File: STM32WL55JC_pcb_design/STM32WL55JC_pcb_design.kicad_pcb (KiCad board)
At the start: 2 copper layers, 131 parts, among them IC1 STM32F051R8T6, IC2 CG2409M2, IC3 SX1276IMLTRT, IC4 CG2409M2, IC5 PCF8575TS_1,118, IC6 PCF8575TS_1,118, IC7 ATGM336H-5N31, J1 Conn_01x03, J10 Conn_01x08_Male, J11 Conn_02x02_Odd_Even, J12 Conn_01x10, J13 Conn_01x10, J14 Conn_01x10, J15 Conn_01x10, J16 Conn_Coaxial, J17 Conn_Coaxial, J18 CT3151-2, J19 CT3151-2, J2 Conn_01x03, J20 USB-A-S-F-B-TH, J21 Conn_02x02_Odd_Even, J22 Conn_01x19_Male, J23 RSP-122811-01, J3 Conn_01x03, J4 Conn_01x09, J5 Conn_01x09, J6 Conn_01x03, J7 Conn_01x09, J8 Conn_01x09, J9 Conn_02x10_Odd_Even, Q1 AO3401A, U1 PCF8574, U2 SHT30-DIS, U3 LIS3DHTR, U4 AMS1117-3.3, U5 AMS1117-5.0, Y1 32MHz, Y2 32.768kHz, Y3 32MHz

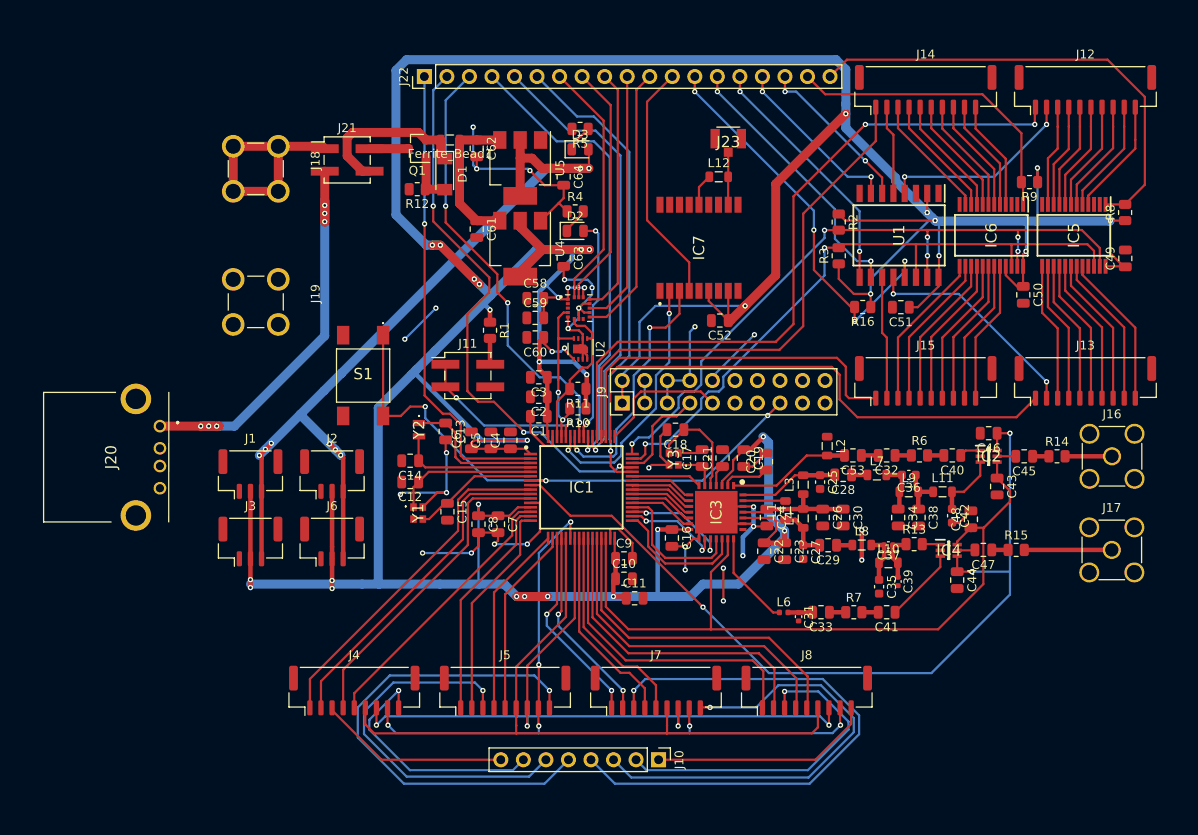
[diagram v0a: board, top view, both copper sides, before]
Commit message: Add copper fill and edge cuts
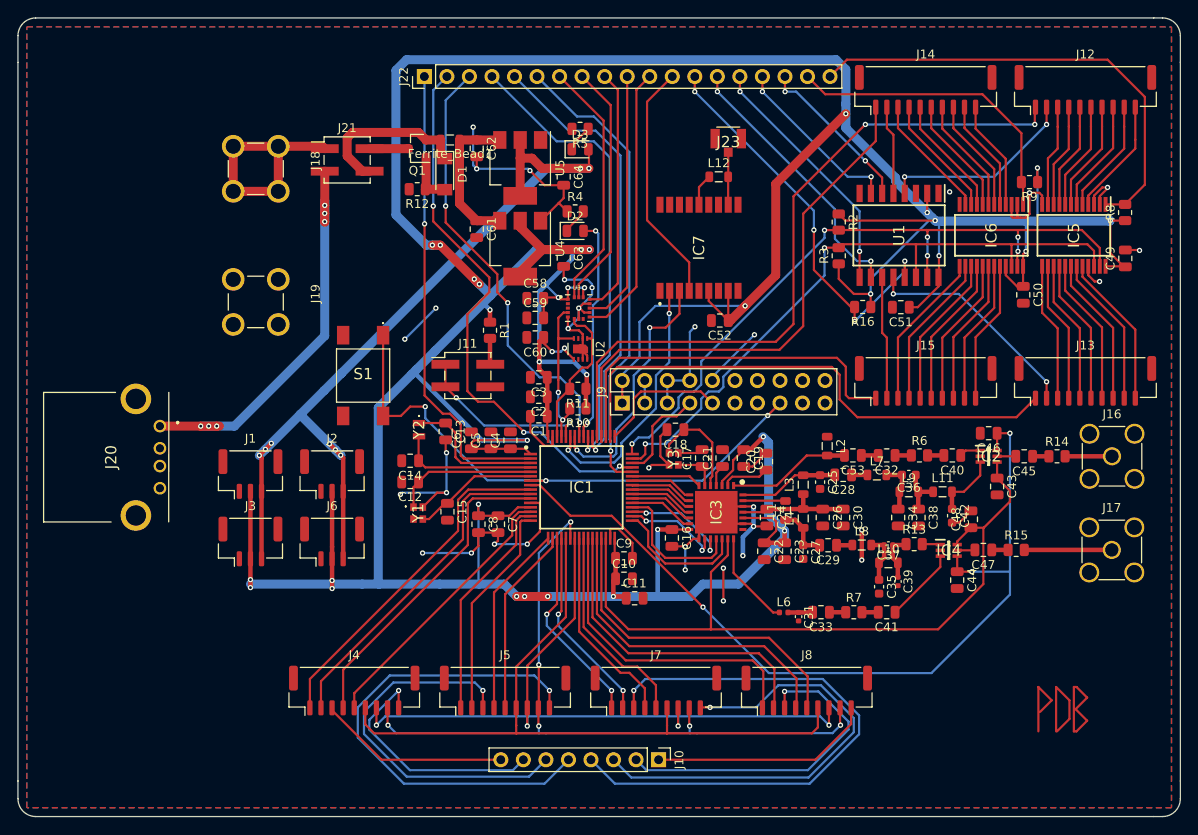
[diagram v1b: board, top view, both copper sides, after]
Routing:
- net (no net): track 0.00 -> 32.8 mm
- net GNDREF: track 172.1 -> 191.6 mm, vias 28 -> 33
- added copper zone on B.Cu, net GNDREF
- added copper zone on F.Cu, net GNDREF
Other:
- board outline added: 131 x 90 mm
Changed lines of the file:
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@@
   (general
     (thickness 1.6)
-    (drawings 0)
-    (tracks 1407)
+    (drawings 14)
+    (tracks 1450)
     (zones 0)
     (modules 131)
@@
     )
   )
+  (gr_line (start 207 121) (end 207 119) (layer Edge.Cuts) (width 0.05))
+  (gr_line (start 76 119) (end 76 121) (layer Edge.Cuts) (width 0.05))
+  (gr_line (start 76 38) (end 76 35) (layer Edge.Cuts) (width 0.05))
+  (gr_line (start 207 38) (end 207 35) (layer Edge.Cuts) (width 0.05))
+  (gr_line (start 204 123) (end 205 123) (layer Edge.Cuts) (width 0.05))
+  (gr_line (start 204 33) (end 205 33) (layer Edge.Cuts) (width 0.05))
+  (gr_line (start 204 123) (end 78 123) (layer Edge.Cuts) (width 0.05))
+  (gr_line (start 207 38) (end 207 119) (layer Edge.Cuts) (width 0.05))
+  (gr_line (start 78 33) (end 204 33) (layer Edge.Cuts) (width 0.05))
+  (gr_line (start 76 119) (end 76 38) (layer Edge.Cuts) (width 0.05))
+  (gr_arc (start 205 35) (end 207 35) (angle -90) (layer Edge.Cuts) (width 0.05))
+  (gr_arc (start 205 121) (end 205 123) (angle -90) (layer Edge.Cuts) (width 0.05))
+  (gr_arc (start 78 121) (end 76 121) (angle -90) (layer Edge.Cuts) (width 0.05))
+  (gr_arc (start 78 35) (end 78 33) (angle -90) (layer Edge.Cuts) (width 0.05))
+  (segment (start 191 108.4) (end 191 113.4) (width 0.25) (layer F.Cu) (net 0))
+  (segment (start 191 108.4) (end 192.5 109.9) (width 0.25) (layer F.Cu) (net 0))
+  (segment (start 192.5 109.9) (end 191.2 111.2) (width 0.25) (layer F.Cu) (net 0))
+  (segment (start 194.5 112) (end 193.1 113.4) (width 0.25) (layer F.Cu) (net 0))
+  (segment (start 194.5 109.9) (end 194.5 112) (width 0.25) (layer F.Cu) (net 0))
+  (segment (start 193 108.4) (end 194.5 109.9) (width 0.25) (layer F.Cu) (net 0))
+  (segment (start 193 113.4) (end 193 108.4) (width 0.25) (layer F.Cu) (net 0))
+  (segment (start 195 108.4) (end 195 113.4) (width 0.25) (layer F.Cu) (net 0))
+  (segment (start 195 108.4) (end 195.3 108.4) (width 0.25) (layer F.Cu) (net 0))
+  (segment (start 195.3 108.4) (end 196.5 109.6) (width 0.25) (layer F.Cu) (net 0))
+  (segment (start 196.5 109.6) (end 195.2 110.9) (width 0.25) (layer F.Cu) (net 0))
+  (segment (start 195.2 110.9) (end 196.5 112.2) (width 0.25) (layer F.Cu) (net 0))
+  (segment (start 195.3 113.4) (end 195 113.4) (width 0.25) (layer F.Cu) (net 0))
+  (segment (start 196.5 112.2) (end 195.3 113.4) (width 0.25) (layer F.Cu) (net 0))
   (via (at 127.1 93.3) (size 0.6) (drill 0.3) (layers F.Cu B.Cu) (net 1))
   (via (at 170.3 67.2) (size 0.6) (drill 0.3) (layers F.Cu B.Cu) (net 172))
@@
   (segment (start 140.7 63) (end 140.7 63.4) (width 0.25) (layer B.Cu) (net 1))
   (segment (start 137.6 62.5) (end 140.2 62.5) (width 0.25) (layer B.Cu) (net 1))
+  (via (at 181 52.6) (size 0.6) (drill 0.3) (layers F.Cu B.Cu) (net 1))
+  (via (at 190 52.7) (size 0.6) (drill 0.3) (layers F.Cu B.Cu) (net 1))
+  (segment (start 191.425 54.012) (end 191.312 54.012) (width 0.25) (layer F.Cu) (net 1))
+  (segment (start 190 55.1) (end 190 52.7) (width 0.25) (layer F.Cu) (net 1))
+  (segment (start 189.6 55.5) (end 190 55.1) (width 0.25) (layer F.Cu) (net 1))
+  (segment (start 189 55.5) (end 189.6 55.5) (width 0.25) (layer F.Cu) (net 1))
+  (segment (start 190 52.7) (end 191.1 52.7) (width 0.25) (layer F.Cu) (net 1))
+  (segment (start 191.425 53.025) (end 191.425 54.012) (width 0.25) (layer F.Cu) (net 1))
+  (segment (start 191.1 52.7) (end 191.425 53.025) (width 0.25) (layer F.Cu) (net 1))
+  (segment (start 187.975 54.012) (end 187.975 55.375) (width 0.25) (layer F.Cu) (net 1))
+  (segment (start 187.975 55.375) (end 188.1 55.5) (width 0.25) (layer F.Cu) (net 1))
+  (segment (start 188.625 55.475) (end 188.6 55.5) (width 0.25) (layer F.Cu) (net 1))
+  (segment (start 188.625 54.012) (end 188.625 55.475) (width 0.25) (layer F.Cu) (net 1))
+  (segment (start 188.6 55.5) (end 189 55.5) (width 0.25) (layer F.Cu) (net 1))
+  (segment (start 188.1 55.5) (end 188.6 55.5) (width 0.25) (layer F.Cu) (net 1))
+  (via (at 198.8 52.1) (size 0.6) (drill 0.3) (layers F.Cu B.Cu) (net 1))
+  (segment (start 197.275 54.012) (end 197.275 53.025) (width 0.25) (layer F.Cu) (net 1))
+  (segment (start 198.2 52.1) (end 198.8 52.1) (width 0.25) (layer F.Cu) (net 1))
+  (segment (start 197.275 53.025) (end 198.2 52.1) (width 0.25) (layer F.Cu) (net 1))
+  (segment (start 198.8 52.2) (end 198.8 52.1) (width 0.25) (layer F.Cu) (net 1))
+  (segment (start 197.925 53.075) (end 198.8 52.2) (width 0.25) (layer F.Cu) (net 1))
+  (segment (start 197.925 54.012) (end 197.925 53.075) (width 0.25) (layer F.Cu) (net 1))
+  (via (at 202.4 59.2) (size 0.6) (drill 0.3) (layers F.Cu B.Cu) (net 1))
+  (segment (start 202.35 59.15) (end 202.4 59.2) (width 0.25) (layer F.Cu) (net 1))
+  (segment (start 200.8 59.15) (end 202.35 59.15) (width 0.25) (layer F.Cu) (net 1))
+  (via (at 197.9 62.7) (size 0.6) (drill 0.3) (layers F.Cu B.Cu) (net 1))
+  (segment (start 197.339498 62.7) (end 197.9 62.7) (width 0.25) (layer F.Cu) (net 1))
+  (segment (start 196.625 61.985502) (end 197.339498 62.7) (width 0.25) (layer F.Cu) (net 1))
+  (segment (start 196.625 60.988) (end 196.625 61.985502) (width 0.25) (layer F.Cu) (net 1))
   (segment (start 166.3875 84.5375) (end 166.4 84.525) (width 0.508) (layer F.Cu) (net 2))
   (segment (start 164.5 84.5375) (end 166.3875 84.5375) (width 0.508) (layer F.Cu) (net 2))
@@
   (segment (start 193.175 47.725) (end 193.175 45.25) (width 0.25) (layer F.Cu) (net 21))
   (segment (start 193.175 45.25) (end 193.175 43.05) (width 0.25) (layer F.Cu) (net 21))
-  (segment (start 201.925 67.912046) (end 201.925 75.85) (width 0.25) (layer F.Cu) (net 22))
-  (segment (start 195.975 61.962046) (end 201.925 67.912046) (width 0.25) (layer F.Cu) (net 22))
-  (segment (start 195.975 60.988) (end 195.975 61.962046) (width 0.25) (layer F.Cu) (net 22))
+  (segment (start 195.975 62.175) (end 201.925 68.125) (width 0.25) (layer F.Cu) (net 22))
+  (segment (start 201.925 68.125) (end 201.925 75.85) (width 0.25) (layer F.Cu) (net 22))
+  (segment (start 195.975 60.988) (end 195.975 62.175) (width 0.25) (layer F.Cu) (net 22))
   (segment (start 195.325 60.988) (end 195.325 62.525) (width 0.25) (layer F.Cu) (net 23))
   (segment (start 195.325 62.525) (end 200.675 67.875) (width 0.25) (layer F.Cu) (net 23))
@@
   (segment (start 131.2 69.9) (end 131.2 65.1) (width 0.25) (layer B.Cu) (net 178))
   (segment (start 139.3 78.6) (end 139.3 75.7) (width 0.25) (layer B.Cu) (net 178))
+  (zone (net 1) (net_name GNDREF) (layer F.Cu) (hatch edge 0.508)
+    (connect_pads (clearance 0.508))
+    (min_thickness 0.254)
+    (fill yes (arc_segments 32) (thermal_gap 0.508) (thermal_bridge_width 0.508))
+    (polygon
+      (pts
+        (xy 206 122) (xy 77 122) (xy 77 34) (xy 206 34)
+      )
+    )
+  )
+  (zone (net 1) (net_name GNDREF) (layer B.Cu) (hatch edge 0.508)
+    (connect_pads (clearance 0.508))
+    (min_thickness 0.254)
+    (fill yes (arc_segments 32) (thermal_gap 0.508) (thermal_bridge_width 0.508))
+    (polygon
+      (pts
+        (xy 206 122) (xy 77 122) (xy 77 34) (xy 206 34)
+      )
+    )
+  )
 )

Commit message: Finish routing
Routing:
- net GNDREF: track 191.6 -> 179.9 mm, vias 33 -> 124
- net PA12: track 62.4 -> 58.2 mm
- net BOOT0: track 20.3 -> 21.4 mm
- net OR1: track 79.2 -> 78.1 mm
- net VDD: track 560.5 -> 559.6 mm
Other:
- rule trace_min: 0.2 -> 0

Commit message: Finish silk screen
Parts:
- removed Ferrite_Bead1: 100@100MHz, Inductor_SMD:L_0805_2012Metric
- added FB1: 100@100MHz, Inductor_SMD:L_0805_2012Metric, F.Cu at (124.7, 46.8)
- added TP1: Micro_VDD, TestPoint:TestPoint_Pad_D4.0mm, B.Cu at (142.4, 102.1)
- added TP11: ACC_VDD, TestPoint:TestPoint_Pad_D2.0mm, B.Cu at (136.5, 66.2)
- added TP12: GND, TestPoint:TestPoint_Pad_D2.0mm, B.Cu at (139.2, 57.0)
- added TP13: Temp_VDD, TestPoint:TestPoint_Pad_D2.0mm, B.Cu at (139.2, 69.4)
- added TP14: GPS_GND, TestPoint:TestPoint_Pad_D4.0mm, B.Cu at (150.4, 48.7)
- added TP15: GPS_VDD, TestPoint:TestPoint_Pad_D4.0mm, B.Cu at (158.1, 61.7)
- added TP2: Micro_GND, TestPoint:TestPoint_Pad_D4.0mm, B.Cu at (149.4, 102.1)
- added TP3: LoRa_VDD, TestPoint:TestPoint_Pad_D4.0mm, B.Cu at (164.1, 80.2)
- added TP4: LoRa_GND, TestPoint:TestPoint_Pad_D4.0mm, B.Cu at (157.6, 84.5)
- added TP5: EXP_VDD1, TestPoint:TestPoint_Pad_D4.0mm, B.Cu at (198.9, 60.0)
- added TP7: EXP_VDD3, TestPoint:TestPoint_Pad_D4.0mm, B.Cu at (178.7, 66.8)
- added TP8: EXP_GND, TestPoint:TestPoint_Pad_D4.0mm, B.Cu at (196.0, 52.8)
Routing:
- net VDD: track 559.6 -> 585.3 mm, vias 36 -> 37
- net GNDREF: track 179.9 -> 182.2 mm, vias 124 -> 131
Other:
- board text added: "1PPS"
- board text added: "ACC"
- board text added: "ADC1"
- board text added: "ADC2"
- board text added: "ADC3"
- board text added: "ADC4"
- board text added: "A_A1"
- board text added: "A_A2"
- board text added: "A_A3"
- board text added: "A_I1"
- board text added: "A_I2"
- board text added: "E1_1"
- board text added: "E1_2"
- board text added: "E2_1"
- board text added: "E2_2"
- board text added: "E3_1"
- board text added: "E3_2"
- board text added: "E4_1"
- board text added: "E4_2"
- board text added: "E_I1"
- board text added: "E_I2"
- board text added: "E_I3"
- board text added: "E_P2"
- board text added: "E_P3"
- board text added: "E_P4"
- board text added: "E_P5"
- board text added: "GND"
- board text added: "GPS"
- board text added: "LoRa"
- board text added: "PA11"
- board text added: "PA12"
- board text added: "PB3"
- board text added: "PB5"
- board text added: "PC13"
- board text added: "PD2"
- board text added: "Paolo de Bruyn"
- board text added: "Plane1"
- board text added: "Plane2"
- board text added: "Plane3"
- board text added: "Plane4"
- board text added: "Power"
- board text added: "ST-Link"
- board text added: "Temp"
- board text added: "VDD"

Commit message: Final push
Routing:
- net +5V: track 45.9 -> 40.1 mm, vias 6 -> 0
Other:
- board text added: "BOOT0"
- board text added: "NRST"
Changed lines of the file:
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@@
   (general
     (thickness 1.6)
-    (drawings 60)
-    (tracks 1589)
+    (drawings 64)
+    (tracks 1573)
     (zones 0)
     (modules 143)
@@
     (34 B.Paste user)
     (35 F.Paste user)
-    (36 B.SilkS user)
-    (37 F.SilkS user)
+    (36 B.SilkS user hide)
+    (37 F.SilkS user hide)
     (38 B.Mask user)
     (39 F.Mask user hide)
@@
     (last_trace_width 0.25)
     (user_trace_width 0.508)
+    (user_trace_width 0.875)
     (user_trace_width 1.016)
+    (user_trace_width 1.451)
+    (user_trace_width 1.524)
     (user_trace_width 2.032)
     (trace_clearance 0.2)
@@
     (tags "Surface mounted pin header SMD 2x02 2.54mm double row")
     (attr smd)
-    (fp_text reference J11 (at 0.55 -3.625) (layer F.SilkS)
+    (fp_text reference J11 (at 0.5 3.4) (layer F.SilkS)
       (effects (font (size 1 1) (thickness 0.15)))
     )
@@
     (tags resistor)
     (attr smd)
-    (fp_text reference R1 (at 0 -1.65 90) (layer F.SilkS)
+    (fp_text reference R1 (at -0.6 -1.65 90) (layer F.SilkS)
       (effects (font (size 1 1) (thickness 0.15)))
     )
@@
     )
   )
+  (gr_text VDD (at 131.2 70.6) (layer F.SilkS)
+    (effects (font (size 1 1) (thickness 0.15)))
+  )
+  (gr_text GND (at 131.2 76.1) (layer F.SilkS)
+    (effects (font (size 1 1) (thickness 0.15)))
+  )
+  (gr_text BOOT0 (at 122.8 69.9) (layer F.SilkS)
+    (effects (font (size 1 1) (thickness 0.15)))
+  )
+  (gr_text NRST (at 114.8 64.8) (layer F.SilkS)
+    (effects (font (size 2 2) (thickness 0.15)))
+  )
   (gr_text E4_1 (at 148.325 120.2 90) (layer F.SilkS)
     (effects (font (size 1 1) (thickness 0.15)))
@@
   (segment (start 195.3 113.4) (end 195 113.4) (width 0.25) (layer F.Cu) (net 0))
   (segment (start 196.5 112.2) (end 195.3 113.4) (width 0.25) (layer F.Cu) (net 0))
-  (via (at 142 62.9) (size 0.6) (drill 0.3) (layers F.Cu B.Cu) (net 1))
+  (via (at 142.1 62.6) (size 0.6) (drill 0.3) (layers F.Cu B.Cu) (net 1))
   (via (at 127.1 93.3) (size 0.6) (drill 0.3) (layers F.Cu B.Cu) (net 1))
   (via (at 158.9 88.05) (size 0.6) (drill 0.3) (layers F.Cu B.Cu) (net 1))
@@
   (segment (start 137.5 61.8) (end 138 62.3) (width 0.508) (layer F.Cu) (net 1))
   (segment (start 137.5 61) (end 137.5 61.8) (width 0.508) (layer F.Cu) (net 1))
-  (via (at 141.8 67.9) (size 0.6) (drill 0.3) (layers F.Cu B.Cu) (net 1))
-  (segment (start 142 65.1) (end 142 62.9) (width 0.25) (layer B.Cu) (net 1))
-  (segment (start 141.8 65.3) (end 142 65.1) (width 0.25) (layer B.Cu) (net 1))
-  (segment (start 141.8 67.9) (end 141.8 65.3) (width 0.25) (layer B.Cu) (net 1))
+  (via (at 142.1 67.8) (size 0.6) (drill 0.3) (layers F.Cu B.Cu) (net 1))
   (via (at 140.6 62.6) (size 0.6) (drill 0.3) (layers F.Cu B.Cu) (net 1))
   (segment (start 140.3 62.3) (end 140.6 62.6) (width 0.25) (layer B.Cu) (net 1))
@@
   (segment (start 140.7 64.2) (end 140.7 62.7) (width 0.25) (layer B.Cu) (net 1))
   (segment (start 139.2 65.7) (end 140.7 64.2) (width 0.25) (layer B.Cu) (net 1))
-  (segment (start 141.7 62.6) (end 142 62.9) (width 0.25) (layer F.Cu) (net 1))
-  (segment (start 140.6 62.6) (end 141.7 62.6) (width 0.25) (layer F.Cu) (net 1))
   (via (at 165.2 62) (size 0.6) (drill 0.3) (layers F.Cu B.Cu) (net 1))
   (via (at 166.8 63.6) (size 0.6) (drill 0.3) (layers F.Cu B.Cu) (net 1))
@@
   (segment (start 146.1 100.4) (end 147.7 100.4) (width 0.25) (layer B.Cu) (net 1))
   (via (at 152.7 100.7) (size 0.6) (drill 0.3) (layers F.Cu B.Cu) (net 1))
+  (segment (start 140.6 62.6) (end 142.1 62.6) (width 0.25) (layer F.Cu) (net 1))
+  (segment (start 142.1 66.1) (end 142.1 62.6) (width 0.25) (layer B.Cu) (net 1))
+  (segment (start 142.1 67.8) (end 142.1 66.1) (width 0.25) (layer B.Cu) (net 1))
   (segment (start 166.3875 84.5375) (end 166.4 84.525) (width 0.508) (layer F.Cu) (net 2))
   (segment (start 164.5 84.5375) (end 166.3875 84.5375) (width 0.508) (layer F.Cu) (net 2))
@@
   (segment (start 201.925 68.125) (end 201.925 75.85) (width 0.25) (layer F.Cu) (net 22))
   (segment (start 195.975 60.988) (end 195.975 62.175) (width 0.25) (layer F.Cu) (net 22))
-  (segment (start 195.325 60.988) (end 195.325 62.525) (width 0.25) (layer F.Cu) (net 23))
-  (segment (start 195.325 62.525) (end 200.675 67.875) (width 0.25) (layer F.Cu) (net 23))
-  (segment (start 200.675 67.875) (end 200.675 75.85) (width 0.25) (layer F.Cu) (net 23))
+  (segment (start 200.675 67.975) (end 200.675 75.85) (width 0.25) (layer F.Cu) (net 23))
+  (segment (start 195.325 62.625) (end 200.675 67.975) (width 0.25) (layer F.Cu) (net 23))
+  (segment (start 195.325 60.988) (end 195.325 62.625) (width 0.25) (layer F.Cu) (net 23))
   (segment (start 194.675 60.988) (end 194.675 63.175) (width 0.25) (layer F.Cu) (net 24))
   (segment (start 194.675 63.175) (end 199.425 67.925) (width 0.25) (layer F.Cu) (net 24))
@@
   (segment (start 142.25 80.162) (end 142.25 72.85) (width 0.25) (layer F.Cu) (net 84))
   (segment (start 189.4125 92.95) (end 199.275 92.95) (width 0.508) (layer F.Cu) (net 85))
-  (segment (start 92 79) (end 96.6 79) (width 1.016) (layer F.Cu) (net 86))
-  (segment (start 97.5 79) (end 97.5 79) (width 1.016) (layer F.Cu) (net 86))
-  (via (at 97.5 79) (size 0.6) (drill 0.3) (layers F.Cu B.Cu) (net 86))
-  (via (at 96.6 79) (size 0.6) (drill 0.3) (layers F.Cu B.Cu) (net 86))
-  (segment (start 96.6 79) (end 98.4 79) (width 1.016) (layer F.Cu) (net 86))
-  (segment (start 98.4 79) (end 98.7 79) (width 1.016) (layer F.Cu) (net 86))
-  (via (at 98.4 79) (size 0.6) (drill 0.3) (layers F.Cu B.Cu) (net 86))
-  (segment (start 110.575 68.825) (end 110.575 53.525) (width 1.016) (layer B.Cu) (net 86))
-  (segment (start 100.4 79) (end 110.575 68.825) (width 1.016) (layer B.Cu) (net 86))
-  (segment (start 96.6 79) (end 100.4 79) (width 1.016) (layer B.Cu) (net 86))
-  (segment (start 110.575 50.27) (end 110.575 54.125) (width 1.016) (layer F.Cu) (net 86))
-  (segment (start 110.575 55.95) (end 110.575 56.025) (width 1.016) (layer F.Cu) (net 86))
-  (via (at 110.575 55.95) (size 0.6) (drill 0.3) (layers F.Cu B.Cu) (net 86))
-  (segment (start 110.575 55.025) (end 110.575 55.95) (width 1.016) (layer F.Cu) (net 86))
-  (via (at 110.575 55.025) (size 0.6) (drill 0.3) (layers F.Cu B.Cu) (net 86))
-  (segment (start 110.575 54.125) (end 110.575 55.025) (width 1.016) (layer F.Cu) (net 86))
-  (via (at 110.575 54.125) (size 0.6) (drill 0.3) (layers F.Cu B.Cu) (net 86))
+  (segment (start 110.575 66.725) (end 110.575 50.27) (width 1.016) (layer F.Cu) (net 86))
+  (segment (start 98.3 79) (end 110.575 66.725) (width 1.016) (layer F.Cu) (net 86))
+  (segment (start 92 79) (end 98.3 79) (width 1.016) (layer F.Cu) (net 86))
   (via (at 138 81.7) (size 0.6) (drill 0.3) (layers F.Cu B.Cu) (net 88))
   (via (at 149.4 66.3) (size 0.6) (drill 0.3) (layers F.Cu B.Cu) (net 88))
@@
   (segment (start 139.75 80.162) (end 139.75 79.05) (width 0.25) (layer F.Cu) (net 155))
   (segment (start 141.1 57) (end 139.7375 57) (width 0.25) (layer F.Cu) (net 155))
-  (segment (start 141.3 57.2) (end 141.1 57) (width 0.25) (layer B.Cu) (net 155))
-  (segment (start 140.8 65.4) (end 141.3 64.9) (width 0.25) (layer B.Cu) (net 155))
-  (segment (start 141.3 64.9) (end 141.3 57.2) (width 0.25) (layer B.Cu) (net 155))
+  (segment (start 141.4 57.3) (end 141.1 57) (width 0.25) (layer B.Cu) (net 155))
+  (segment (start 141.4 64.8) (end 141.4 57.3) (width 0.25) (layer B.Cu) (net 155))
+  (segment (start 140.8 65.4) (end 141.4 64.8) (width 0.25) (layer B.Cu) (net 155))
   (segment (start 140.8 78) (end 140.8 65.4) (width 0.25) (layer B.Cu) (net 155))
   (segment (start 140.2 78.6) (end 140.8 78) (width 0.25) (layer B.Cu) (net 155))
@@
   (segment (start 173.395 52.775) (end 173.395 50.995) (width 0.25) (layer F.Cu) (net 174))
   (segment (start 173.395 50.995) (end 171.5 49.1) (width 0.25) (layer F.Cu) (net 174))
-  (segment (start 163.7 41.3) (end 171.5 49.1) (width 0.25) (layer B.Cu) (net 174))
-  (segment (start 162.45 41.3) (end 163.7 41.3) (width 0.25) (layer B.Cu) (net 174))
+  (segment (start 170.25 49.1) (end 171.5 49.1) (width 0.25) (layer B.Cu) (net 174))
+  (segment (start 162.45 41.3) (end 170.25 49.1) (width 0.25) (layer B.Cu) (net 174))
   (via (at 154.825 41.3) (size 0.6) (drill 0.3) (layers F.Cu B.Cu) (net 175))
   (via (at 172.125 60.4) (size 0.6) (drill 0.3) (layers F.Cu B.Cu) (net 175))
